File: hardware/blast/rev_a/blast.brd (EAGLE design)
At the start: 32.5 x 13 mm, 35 parts, among them J2 TC2030-CTX-NL, J3 IMPULSE_GECKO_HEADER, Q1 MOSFET-NCHANNELXFDN-3, U2 FM25LBTDFN-8, U3 NRF51822QF, X2 16MHz

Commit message: blast routed
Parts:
- added C1: 0.8pF, passives:0402_CAP
- J1: value TC2030-CTX-NL -> TC2030-JLINK-NL
- L1: device SparkFun-Passives:0603 -> passives:0603_CAP
- L2: value INDUCTOR0402 -> (none)
- moved R1 10.3 mm to (26.6, 12.3)
- moved D1 10.2 mm to (24.2, 12.3)
- moved C3 2.73 mm to (18.5, 2.26), turned to 0 degrees
- moved C7 2.64 mm to (17.6, 11.3), turned to 90 degrees
- moved C6 2.34 mm to (18.8, 4.59)
- moved L2 2.25 mm to (18.5, 1.24), turned to 0 degrees
- moved R6 1.92 mm to (19.6, 12.0), turned to 180 degrees
- moved C16 1.86 mm to (19.8, 9.76), turned to 0 degrees
- moved L1 1.55 mm to (20.5, 1.88)
- moved R5 1.53 mm to (24.4, 4.01), turned to 270 degrees
- moved Q1 1.31 mm to (19.6, 11.0), turned to 0 degrees
- moved C12 1.27 mm to (10.5, 9.53)
- moved R7 1.24 mm to (21.4, 11.2), turned to 270 degrees
- moved R8 1.17 mm to (10.8, 11.7)
- moved R3 1.15 mm to (22.7, 4.34)
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- renumbered J2 to J1
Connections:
- removed net !RESET: J1.3
- removed net TCK: J1.4
- removed net TDO: J1.6
- removed net TMS: J1.2
- net !FRAM_CS: now also U3.4; no longer U3.6
- net !FRAM_HOLD: now also U3.6; no longer U3.5
- net !FRAM_WP: now also U3.5; no longer U3.4
- net GND: now also C1.2; no longer D1.C, D2.C
- net N$1: now also D2.C, U3.21; no longer R2.1, U3.16
- net N$11: now also C1.1
- net N$7: now also D1.C, U3.16; no longer R1.1, U3.15
- net SWDCLK: now also J1.4
- net SWDIO: now also J1.2
- net VCC: now also R1.1, R2.1
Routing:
- net VCC: track 0.00 -> 49.3 mm, vias 0 -> 7
- net SWDCLK: track 0.00 -> 26.7 mm, vias 0 -> 2
- net SCK: track 0.00 -> 25.6 mm, vias 0 -> 2
- net SWDIO: track 0.00 -> 24.5 mm, vias 0 -> 2
- net MOSI: track 0.00 -> 21.2 mm, vias 0 -> 2
- net MISO: track 0.00 -> 18.5 mm, vias 0 -> 2
- net OV: track 0.00 -> 13.9 mm, vias 0 -> 2
- net GND: track 0.00 -> 13.0 mm, vias 0 -> 33
- net SHDN: track 0.00 -> 12.5 mm, vias 0 -> 2
- net TRIG: track 0.00 -> 11.9 mm, vias 0 -> 2
- net N$12: track 0.00 -> 11.5 mm, vias 0 -> 2
- net N$7: track 0.00 -> 9.81 mm
- net !FRAM_HOLD: track 0.00 -> 8.54 mm
- net !FRAM_WP: track 0.00 -> 8.50 mm
- net !FRAM_CS: track 0.00 -> 6.58 mm
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- removed copper zone on layer 2, net GND
- removed copper zone on layer 15, net VCC
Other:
- board text added: "2014/10/03"
- board text removed: "2013/08/14"

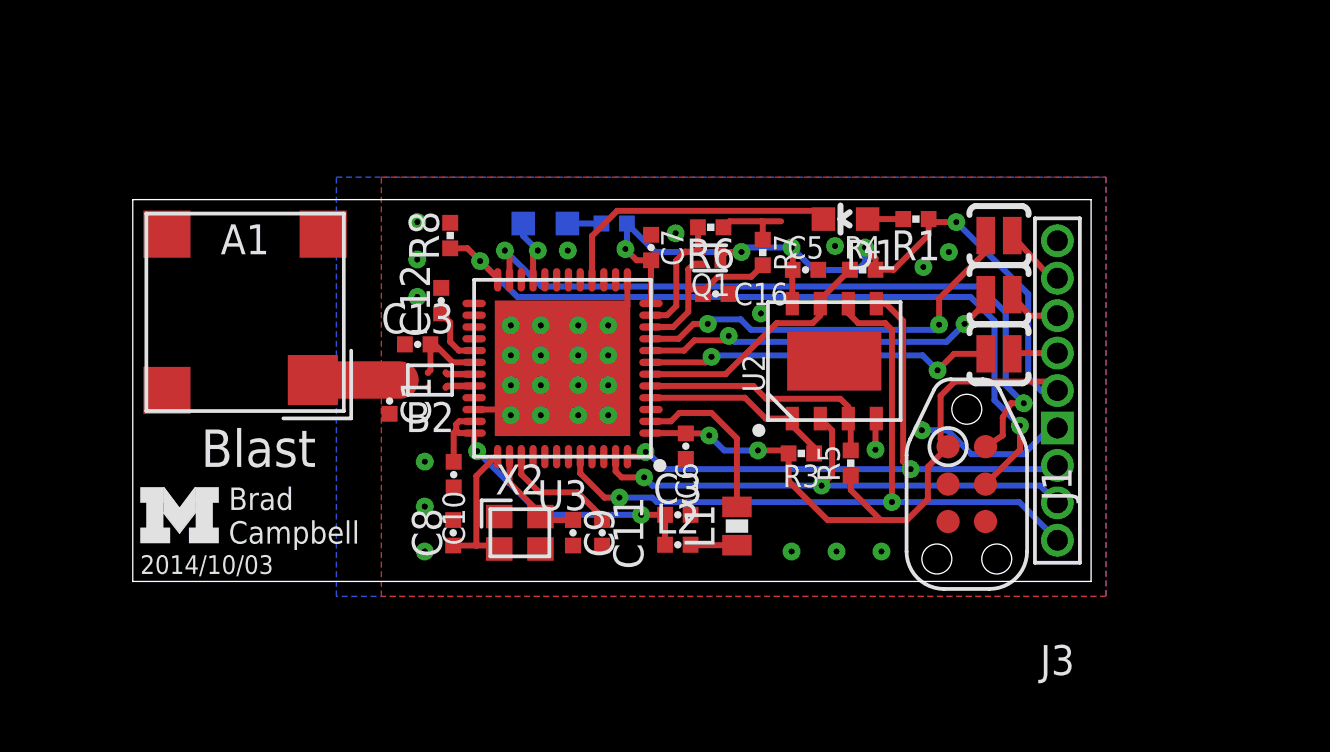
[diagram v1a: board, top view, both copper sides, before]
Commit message: update to bigger solar panel
- add footprint for big fram
- add footprint for rtc
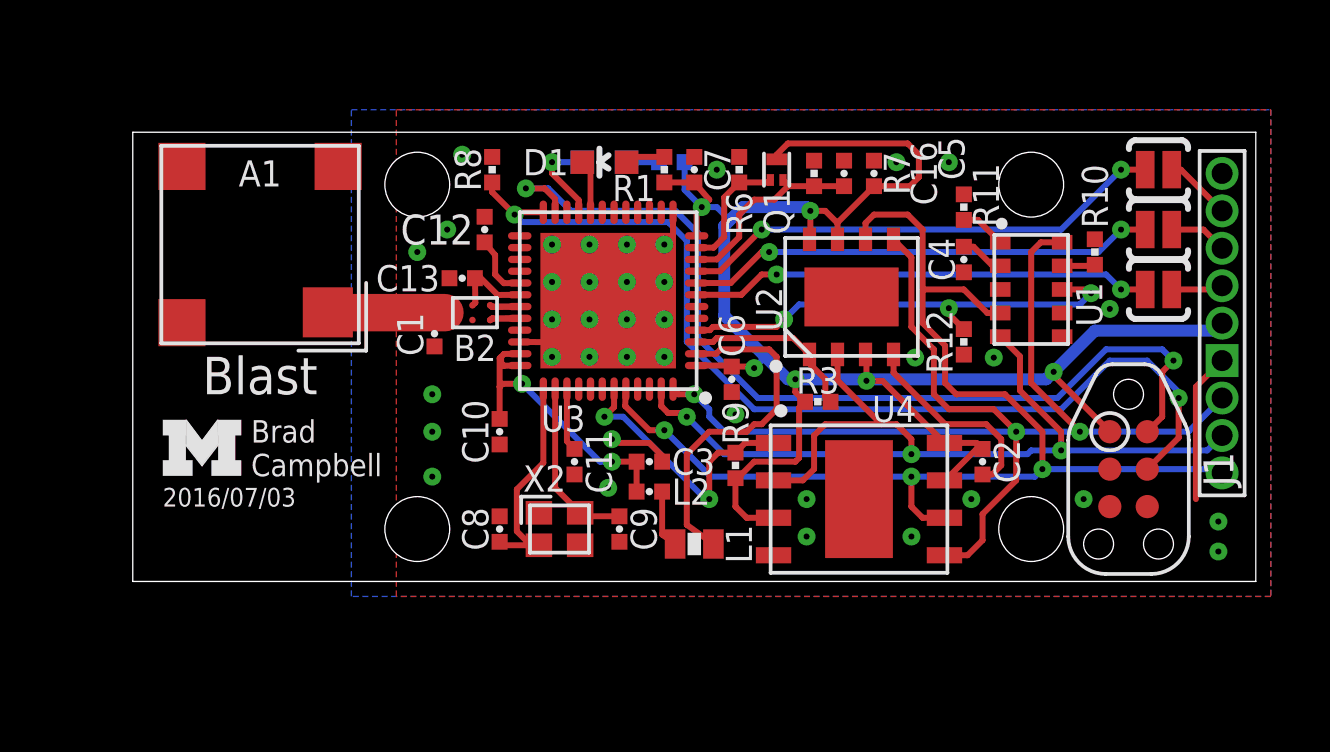
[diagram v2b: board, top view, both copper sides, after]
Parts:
- removed R4, R5: 4.7k, passives:0402_RES
- added C2: 0.1uF, passives:0402_CAP
- added C4: 10nF, passives:0402_CAP
- added R10, R11: 10k, passives:0402_RES
- added R12, R9: 4.7k, passives:0402_RES
- added U1: RV-3049-C3, chips:MICRO-CRYSTAL-C3
- added U4: FM25V20-DG, chips:TDFN-8/6MM
- U2: device chips:TDFN-8 -> chips:TDFN-8@1
- moved R1 8.70 mm to (18.0, 14.0), turned to 90 degrees
- moved D1 8.40 mm to (16.0, 14.2)
- moved J3 6.04 mm to (37.0, 8.76)
- moved C16 5.97 mm to (24.1, 13.8), turned to 90 degrees
- moved SJ1 5.85 mm to (34.8, 14.0)
- moved SJ2 5.84 mm to (34.8, 11.9)
- moved SJ3 5.83 mm to (34.8, 9.91)
- moved J1 5.51 mm to (33.8, 3.81)
- moved C5 4.01 mm to (25.1, 13.8), turned to 90 degrees
- moved Q1 3.75 mm to (21.8, 14.0), turned to 90 degrees
- moved R7 3.20 mm to (23.1, 13.8)
- moved C7 3.02 mm to (19.1, 14.0)
- moved D2 2.89 mm to (16.0, 14.2)
- moved R2 2.86 mm to (18.3, 14.2)
- moved C12 2.83 mm to (11.9, 11.9)
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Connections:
- new net !FRAM2_CS: R9.1, U3.43, U4.1
- new net BATTERY: C4.1, U1.2
- new net N$8: R10.2, U1.9
- new net N$9: R11.2, U1.1
- new net RTC_CS: R12.2, U1.8, U3.4
- net !FRAM_CS: now also U3.3; no longer U3.4
- net !FRAM_HOLD: no longer R4.1, U2.7
- net !FRAM_WP: no longer R5.1, U2.3
- net GND: now also C2.2, C4.2, R10.1, R11.1, R12.1, U1.6, U4.4
- net MISO: now also U1.5, U4.2
- net MOSI: now also U1.10, U4.5
- net N$7: now also U3.20; no longer U3.16
- net SCK: now also U1.4, U4.6
- net VCC: now also C2.1, R9.2, U2.3, U2.7, U4.3, U4.7, U4.8; no longer R4.2, R5.2
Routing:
- net MOSI: track 21.2 -> 42.6 mm, vias 2 -> 3
- net VCC: track 49.3 -> 66.2 mm, vias 7 -> 6
- net MISO: track 18.5 -> 35.1 mm, vias 2 -> 3
- net RTC_CS: track 0.00 -> 16.0 mm, vias 0 -> 3
- net SCK: track 25.6 -> 40.8 mm, vias 2 -> 3
- net !FRAM2_CS: track 0.00 -> 9.50 mm, vias 0 -> 2
- net !FRAM_HOLD: track 8.54 -> 0.00 mm
- net !FRAM_WP: track 8.50 -> 0.00 mm
- net N$7: track 9.81 -> 1.81 mm
- net SWDIO: track 24.5 -> 32.2 mm
- net SWDCLK: track 26.7 -> 33.9 mm
- net N$13: track 5.71 -> 11.9 mm
- net GND: track 13.0 -> 18.8 mm, vias 33 -> 38
- net TRIG: track 11.9 -> 15.7 mm
- net SHDN: track 12.5 -> 16.0 mm
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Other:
- board size 32.5 x 13 mm -> 38.1 x 15.2 mm
- board text added: "2016/07/03"
- board text removed: "2014/10/03"

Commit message: add blast files
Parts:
- removed C16: 2.2uF, passives:0402_CAP
- removed J3: IMPULSE_GECKO_HEADER, gecko:HEADER1X9/0.05IN
- removed R11: 10k, passives:0402_RES
- removed R12: 4.7k, passives:0402_RES
- added C14: 4.7uF, passives:0402_CAP
- added J2: TC2030-JLINK-NL, connector:TC2030-IDC-NL
- added R4, R5: 4.7k, passives:0402_RES
- added SJ4: SOLDERJUMPERNO, SparkFun-Passives:SJ_2S-NO
- C10, C11: value 1nF -> 0.1uF
- C12: value 47nF -> 1uF
- C13: value 2.2nF -> 2.2uF
- C2: value 0.1uF -> 12pF
- C3: value 1uF -> 12pF
- C4: value 10nF -> 1nF
- C5: value 0.1uF -> 1nF
- C6: value 4.7uF -> 2.2nF
- C7: value 0.1uF -> 10nF
- C8: value 12pF -> 47nF
- C9: value 12pF -> 0.1uF
- J1: value TC2030-JLINK-NL -> IMPULSE_GECKO_HEADER; device connector:TC2030-IDC-NL -> gecko:HEADER1X9/0.05IN
- L2: value (none) -> 15nH
- R10: value 10k -> 4.7M
- R6: value 1M -> 10k
- R7: value 4.7M -> 10k
- R9: value 4.7k -> 1M
- U1: value RV-3049-C3 -> NRF51822QF; device chips:MICRO-CRYSTAL-C3 -> chips:QFN-48-6MM
- U3: value NRF51822QF -> RV-3049-C3; device chips:QFN-48-6MM -> chips:MICRO-CRYSTAL-C3
- moved C4 16.8 mm to (12.4, 5.08)
- moved C2 16.5 mm to (12.4, 1.78), turned to 90 degrees
- moved C10 15.4 mm to (25.1, 13.8), turned to 90 degrees
- moved U1 14.4 mm to (16.1, 9.53), turned to 180 degrees
- moved U3 14.4 mm to (30.5, 9.53), turned to 270 degrees
- moved C5 14.1 mm to (15.0, 4.06), turned to 270 degrees
- moved C11 13.8 mm to (28.8, 4.06)
- moved C13 13.4 mm to (24.1, 13.8), turned to 90 degrees
- moved C9 12.5 mm to (19.1, 14.0), turned to 90 degrees
- moved C7 10.4 mm to (28.1, 8.84), turned to 270 degrees
- moved R7 10.3 mm to (33.0, 10.9), turned to 180 degrees
- moved C8 10.2 mm to (11.9, 11.9)
- moved R9 10.0 mm to (20.6, 14.0)
- moved R10 9.89 mm to (23.1, 13.8)
- moved C6 9.77 mm to (11.2, 10.3), turned to 180 degrees
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- renumbered B2 to B1, X2 to X1
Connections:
- removed net !FRAM_HOLD: U3.6
- removed net !FRAM_WP: U3.5
- net !FRAM2_CS: now also R4.1, U1.43; no longer R9.1, U3.43
- net !FRAM_CS: now also U1.3; no longer U3.3
- net BATTERY: now also C7.1, SJ4.1, U3.2; no longer C4.1, U1.2
- net GND: now also C14.2, J1.0, J2.5, R5.1, R9.1, U1.13, U1.33, U1.34, U1.GND, U3.6; no longer C16.2, J1.5, J3.0, R11.1, R12.1, U1.6, U3.13, U3.33, U3.34, U3.GND
- net MISO: now also J1.-2, U1.47, U3.5; no longer J3.-2, U1.5, U3.47
- net MOSI: now also J1.-1, U1.48, U3.10; no longer J3.-1, U1.10, U3.48
- net N$1: now also U1.21; no longer U3.21
- net N$12: now also C12.1, C4.1, U1.35, U1.36; no longer C10.1, C3.1, U3.35, U3.36
- net N$13: now also U1.2; no longer U3.2
- net N$16: now also C2.1, U1.37; no longer C8.1, U3.37
- net N$17: now also C3.1, U1.38; no longer C9.1, U3.38
- net N$18: now also C5.1, U1.39; no longer C11.1, U3.39
- net N$19: now also C8.1, U1.29; no longer C12.1, U3.29
- net N$20: now also J1.2; no longer J3.2
- net N$21: now also J1.3; no longer J3.3
- net N$22: now also J1.4; no longer J3.4
- net N$5: now also U1.31; no longer U3.31
- net N$6: now also U1.32; no longer U3.32
- net N$7: now also U1.20; no longer U3.20
- net N$8: now also R7.2, U3.9; no longer R10.2, U1.9
- net N$9: now also R6.2, U3.1; no longer R11.2, U1.1
- net OV: now also U1.9; no longer U3.9
- net RTC_CS: now also R5.2, U1.4, U3.8; no longer R12.2, U1.8, U3.4
- net SCK: now also J1.-3, U1.44, U3.4; no longer J3.-3, U1.4, U3.44
- net SHDN: now also U1.8; no longer U3.8
- net SWDCLK: now also J2.4, U1.24; no longer J1.4, U3.24
- net SWDIO: now also J2.2, U1.23; no longer J1.2, U3.23
- net TIME_CTL: now also R9.2, U1.11; no longer R6.2, U3.11
- net TRIG: now also U1.7; no longer U3.7
- net VCAP: now also J1.5, SJ4.2; no longer J3.5
- net VCC: now also C10.1, C11.1, C14.1, C9.1, J2.1, R4.2, U1.1, U1.12; no longer C2.1, C5.1, C6.1, C7.1, J3.1, R9.2, U3.1, U3.12
- net VDD_PA: now also C6.1, U1.30; no longer C13.1, U3.30
- net VTIMER: now also C13.1, R10.2, U1.10; no longer C16.1, R7.2, U3.10
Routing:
- net VCAP: track 0.00 -> 13.8 mm, vias 0 -> 1
- net BATTERY: track 1.50 -> 6.30 mm
- net OV: track 16.6 -> 18.0 mm
- net RTC_CS: track 16.0 -> 17.2 mm, vias 3 -> 2
- net GND: track 18.8 -> 19.8 mm
- net SHDN: track 16.0 -> 16.8 mm
- net MOSI: track 42.6 -> 42.1 mm
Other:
- board text added: "Activator"
- board text added: "OV"
- board text added: "RTC"
- board text added: "SHDN"
- board text added: "TRG"
- board text added: "VCAP"
